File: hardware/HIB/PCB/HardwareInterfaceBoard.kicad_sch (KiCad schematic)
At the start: 81 parts, among them J1 Relay Board Connector, J11 Feed Sensor R2, J14 Left LEDs, J15 Right LEDs, J16 Reset, J17 Shutdown, J2 Pi 5V, J20 EXT, J24 Raspberry Pi GPIO header, J25 RTC Header, J26 I2C0, J27 I2C1, J28 I2C2, J29 I2C3, J3 Display 5V, J30 I2C4, J31 I2C5, J32 I2C6, J33 I2C7, J4 DC 5V, J5 GPIO, J6 Feed Sensor L1, J7 Power bus, J8 Feed Sensor R1, J9 Feed Sensor L2, Q1 PN2222A, Q2 PN2222A, Q3 PN2222A, Q4 PN2222A, Q5 PN2222A, Q6 PN2222A, Q7 PN2222A, Q8 PN2222A, Q9 TP0610L, SW1 Pico Reset, U1 Raspberry Pico, U2 74HC595, U3 TCA9548A, U4 LM1117, U5 DS3231MZ, U6 74HC165, U7 74HC165

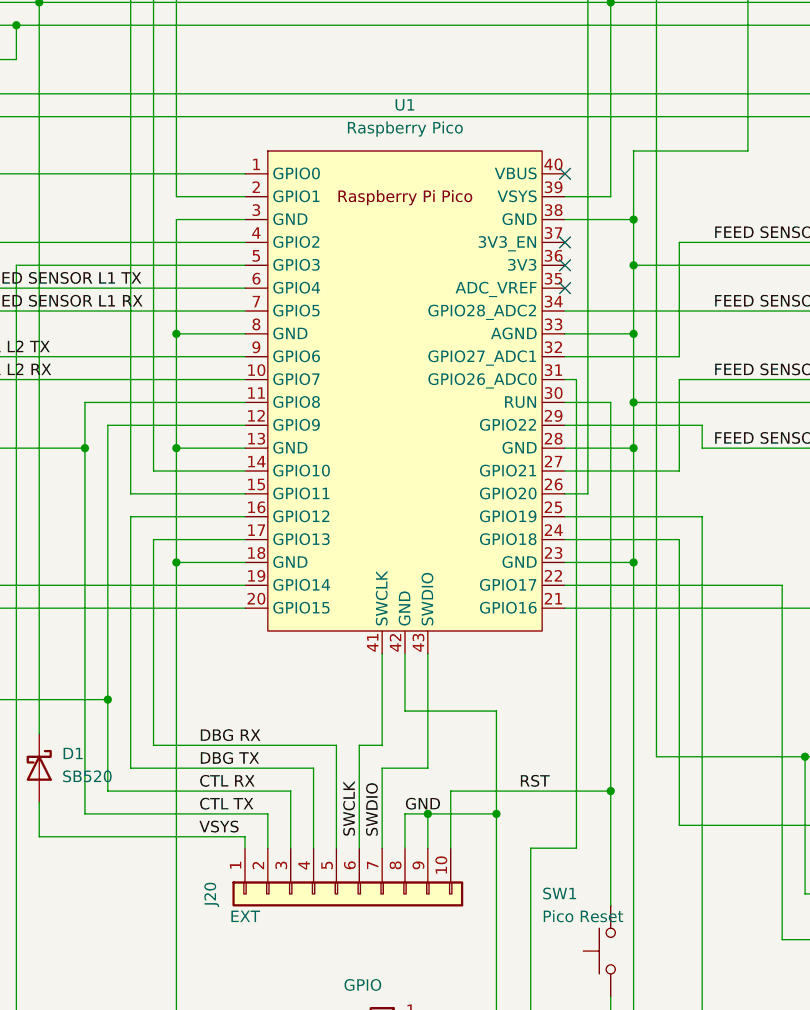
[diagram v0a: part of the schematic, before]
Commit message: Fixed up paths for extra device symbols/models. Swapped HIB design over to Pico W footprint
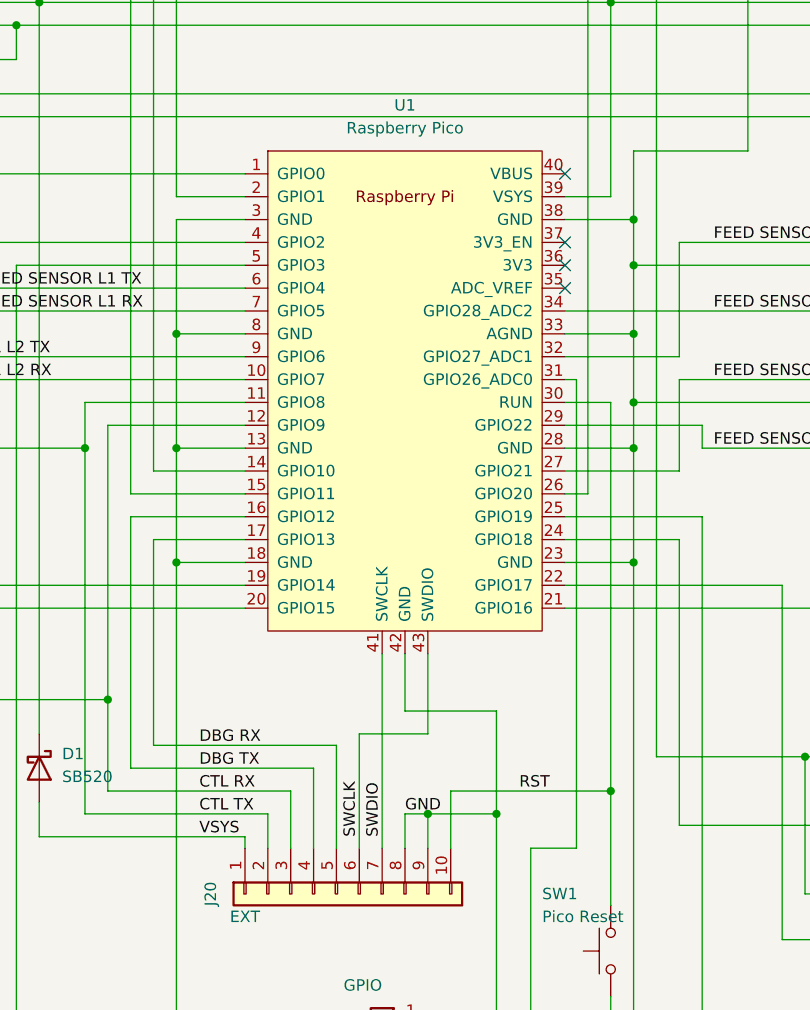
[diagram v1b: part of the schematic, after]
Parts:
- U1: footprint MCU_RaspberryPi_and_Boards:RPi_Pico_SMD_TH -> RPi_Pico:RPi_PicoW_SMD_TH; symbol MCU_RaspberryPi_and_Boards:Pico -> RPi_Pico:PicoW
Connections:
- net SWCLK: now also U1.43 (SWDIO); no longer U1.41 (SWCLK)
- net SWDIO: now also U1.41 (SWCLK); no longer U1.43 (SWDIO)
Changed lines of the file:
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@@
     (stroke (width 0) (type default) (color 0 0 0 0))
   )
-  (wire (pts (xy 275.59 274.32) (xy 278.13 274.32))
-    (stroke (width 0) (type default) (color 0 0 0 0))
-  )
   (wire (pts (xy 246.38 171.45) (xy 288.29 171.45))
     (stroke (width 0) (type default) (color 0 0 0 0))
@@
     (stroke (width 0) (type default) (color 0 0 0 0))
   )
-  (wire (pts (xy 283.21 276.86) (xy 283.21 264.16))
-    (stroke (width 0) (type default) (color 0 0 0 0))
-  )
   (wire (pts (xy 148.59 111.76) (xy 165.1 111.76))
     (stroke (width 0) (type default) (color 0 0 0 0))
@@
     (stroke (width 0) (type default) (color 0 0 0 0))
   )
+  (wire (pts (xy 275.59 273.05) (xy 283.21 273.05))
+    (stroke (width 0) (type default) (color 0 0 0 0))
+  )
   (wire (pts (xy 264.16 113.03) (xy 391.16 113.03))
     (stroke (width 0) (type default) (color 0 0 0 0))
@@
     (stroke (width 0) (type default) (color 0 0 0 0))
   )
-  (wire (pts (xy 278.13 285.75) (xy 278.13 276.86))
-    (stroke (width 0) (type default) (color 0 0 0 0))
-  )
   (wire (pts (xy 298.45 241.3) (xy 306.07 241.3))
     (stroke (width 0) (type default) (color 0 0 0 0))
@@
     (stroke (width 0) (type default) (color 0 0 0 0))
   )
-  (wire (pts (xy 278.13 264.16) (xy 278.13 274.32))
+  (wire (pts (xy 278.13 264.16) (xy 278.13 285.75))
     (stroke (width 0) (type default) (color 0 0 0 0))
   )
@@
     (stroke (width 0) (type default) (color 0 0 0 0))
   )
-  (wire (pts (xy 278.13 276.86) (xy 283.21 276.86))
-    (stroke (width 0) (type default) (color 0 0 0 0))
-  )
   (wire (pts (xy 458.47 196.85) (xy 458.47 200.66))
     (stroke (width 0) (type default) (color 0 0 0 0))
@@
     (stroke (width 0) (type default) (color 0 0 0 0))
   )
+  (wire (pts (xy 283.21 273.05) (xy 283.21 264.16))
+    (stroke (width 0) (type default) (color 0 0 0 0))
+  )
   (wire (pts (xy 363.22 67.31) (xy 363.22 69.85))
     (stroke (width 0) (type default) (color 0 0 0 0))
@@
     (stroke (width 0) (type default) (color 0 0 0 0))
   )
-  (wire (pts (xy 275.59 285.75) (xy 275.59 274.32))
+  (wire (pts (xy 275.59 273.05) (xy 275.59 285.75))
     (stroke (width 0) (type default) (color 0 0 0 0))
   )
@@
     (pin "5")
   )
-  (symbol (lib_id "MCU_RaspberryPi_and_Boards:Pico") (at 280.67 234.95 0) (unit 1)
+  (symbol (lib_id "RPi_Pico:PicoW") (at 280.67 234.95 0) (unit 1)
     (in_bom yes) (on_board yes) (fields_autoplaced)
     (property "Reference" "U1" (id 0) (at 280.67 203.2 0))
     (property "Value" "Raspberry Pico" (id 1) (at 280.67 205.74 0))
-    (property "Footprint" "MCU_RaspberryPi_and_Boards:RPi_Pico_SMD_TH" (id 2) (at 280.67 234.95 90)
+    (property "Footprint" "RPi_Pico:RPi_PicoW_SMD_TH" (id 2) (at 280.67 234.95 90)
       (effects (font (size 1.27 1.27)) hide)
     )
@@
     )
     (path "/ee08b670-97de-4511-a243-fc32575f8109"
-      (reference "U1") (unit 1) (value "Raspberry Pico") (footprint "MCU_RaspberryPi_and_Boards:RPi_Pico_SMD_TH")
+      (reference "U1") (unit 1) (value "Raspberry Pico") (footprint "RPi_Pico:RPi_PicoW_SMD_TH")
     )
     (path "/12cf374e-e012-4dc5-bbe9-33f8c02cf6dc"
